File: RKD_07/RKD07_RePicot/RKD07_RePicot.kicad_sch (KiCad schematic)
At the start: 13 parts, among them J1 Conn_01x06, J2 Conn_01x24, J3 Qwiic_RA, J4 Conn_01x06, J5 Conn_01x02_Socket, J6 Conn_01x06, J8 Conn_01x06, SW41 SW_Push, U1 Pico

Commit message: modify
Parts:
- added J7: Conn_01x02_Socket, Connector_PinHeader_2.54mm:PinHeader_1x02_P2.54mm_Horizontal, symbol Connector_Generic:Conn_01x02
- J5: footprint Connector_PinHeader_2.54mm:PinHeader_1x02_P2.54mm_Vertical -> Connector_PinHeader_2.54mm:PinHeader_1x02_P2.54mm_Horizontal
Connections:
- net GP04: now also J7.1 (Pin_1)
- net GP07: now also J7.2 (Pin_2)
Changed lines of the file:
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@@
+		)
+	)
+	(global_label "GP04"
+		(shape input)
+		(at 298.45 120.65 180)
+		(fields_autoplaced yes)
+		(effects
+			(font
+				(size 1.27 1.27)
+			)
+			(justify right)
+		)
+		(property "Intersheetrefs" "${INTERSHEET_REFS}"
+			(at 290.5058 120.65 0)
+			(effects
+				(font
+					(size 1.27 1.27)
+				)
+				(justify right)
+				(hide yes)
+			)
 		)
 	)
@@
 				)
 				(justify left)
+				(hide yes)
+			)
+		)
+	)
+	(global_label "GP07"
+		(shape input)
+		(at 298.45 123.19 180)
+		(fields_autoplaced yes)
+		(effects
+			(font
+				(size 1.27 1.27)
+			)
+			(justify right)
+		)
+		(property "Intersheetrefs" "${INTERSHEET_REFS}"
+			(at 290.5058 123.19 0)
+			(effects
+				(font
+					(size 1.27 1.27)
+				)
+				(justify right)
 				(hide yes)
 			)
@@
 	)
 	(symbol
+		(lib_id "Connector_Generic:Conn_01x02")
+		(at 303.53 120.65 0)
+		(unit 1)
+		(exclude_from_sim no)
+		(in_bom yes)
+		(on_board yes)
+		(dnp no)
+		(fields_autoplaced yes)
+		(property "Reference" "J7"
+			(at 306.07 120.6499 0)
+			(effects
+				(font
+					(size 1.27 1.27)
+				)
+				(justify left)
+			)
+		)
+		(property "Value" "Conn_01x02_Socket"
+			(at 306.07 123.1899 0)
+			(effects
+				(font
+					(size 1.27 1.27)
+				)
+				(justify left)
+			)
+		)
+		(property "Footprint" "Connector_PinHeader_2.54mm:PinHeader_1x02_P2.54mm_Horizontal"
+			(at 303.53 120.65 0)
+			(effects
+				(font
+					(size 1.27 1.27)
+				)
+				(hide yes)
+			)
+		)
+		(property "Datasheet" "~"
+			(at 303.53 120.65 0)
+			(effects
+				(font
+					(size 1.27 1.27)
+				)
+				(hide yes)
+			)
+		)
+		(property "Description" "Generic connector, single row, 01x02, script generated (kicad-library-utils/schlib/autogen/connector/)"
+			(at 303.53 120.65 0)
+			(effects
+				(font
+					(size 1.27 1.27)
+				)
+				(hide yes)
+			)
+		)
+		(pin "1"
+		)
+		(pin "2"
+		)
+		(instances
+			(project "RKD07_RePicot"
+				(path "/237aa5e6-259c-459d-b408-55413a51412a"
+					(reference "J7")
+					(unit 1)
+				)
+			)
+		)
+	)
+	(symbol
 		(lib_id "SparkFun-Connector:Qwiic_Right_Angle")
 		(at 224.79 62.23 0)
@@
 			)
 		)
-		(property "Footprint" "Connector_PinHeader_2.54mm:PinHeader_1x02_P2.54mm_Vertical"
+		(property "Footprint" "Connector_PinHeader_2.54mm:PinHeader_1x02_P2.54mm_Horizontal"
 			(at 304.8 109.22 0)
 			(effects

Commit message: RePicot修正
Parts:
- added C1, C4: 0.1uF, Capacitor_SMD:C_0805_2012Metric_Pad1.18x1.45mm_HandSolder, symbol Device:C_Small
- added C2: 1uF, Capacitor_SMD:C_0805_2012Metric_Pad1.18x1.45mm_HandSolder, symbol Device:C_Small
- added C3: 4.7uF/10V, Capacitor_SMD:C_0805_2012Metric_Pad1.18x1.45mm_HandSolder, symbol Device:C_Small
- added J10, J11: Conn_01x02_Socket, Connector_PinHeader_2.54mm:PinHeader_1x02_P2.54mm_Horizontal, symbol Connector_Generic:Conn_01x02
- added J12: Conn_01x06, Connector_PinHeader_2.54mm:PinHeader_1x06_P2.54mm_Horizontal, symbol Connector_Generic:Conn_01x06
- added J9: Conn_01x06, Connector_FFC-FPC:Hirose_FH12-6S-0.5SH_1x06-1MP_P0.50mm_Horizontal, symbol Connector_Generic:Conn_01x06
- added R3, R5: 10k, Resistor_SMD:R_0805_2012Metric_Pad1.20x1.40mm_HandSolder, symbol Device:R
- added R4: 39R, Resistor_SMD:R_0805_2012Metric_Pad1.20x1.40mm_HandSolder, symbol Device:R
- added U2: TLV70019DDCR, Package_TO_SOT_SMD:SOT-23-5_HandSoldering, symbol Regulator_Linear:TLV70019_SOT23-5
- added U3: PMW3360DM-T2QU, Rikkodo_FootPrint:PMW3360DM-T2QU, symbol sumi-symbols:PMW3360DM-T2QU
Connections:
- net 3V3: now also C1.1, J12.6 (Pin_6), J9.1 (Pin_1), R3.2, R5.1, U2.1 (IN), U2.3 (EN), U3.5 (VDDIO)
- net GND: now also C1.2, C2.2, C3.2, C4.2, J12.1 (Pin_1), J12.2 (Pin_2), J9.6 (Pin_6), U2.2 (GND), U3.13 (NCS), U3.8 (GND)
- net GP00_MISO: now also J12.3 (Pin_3), J9.2 (Pin_2), R5.2, U3.12 (MISO)
- net GP02_SCLK: now also J12.4 (Pin_4), J9.4 (Pin_4), U3.10 (SCLK)
- net GP03_MOSI: now also J12.5 (Pin_5), J9.5 (Pin_5), U3.11 (MOSI)
- new net: C3.1, C4.1, U3.3 (VDDPIX)
- new net: R3.1, U3.7 (NRESET)
- new net: R4.2, U3.15 (LED_P)
- new net +1V9: C2.1, R4.1, U2.5 (OUT), U3.4 (VDD)
- new net GP04_F: J10.1 (Pin_1), J11.2 (Pin_2)
- new net GP07_F: J10.2 (Pin_2), J11.1 (Pin_1)
- no-connect marks 14 -> 16
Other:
- note added: "Nogikesuya_TrackBall"
- moved on the sheet: D41, J1, J2, J3, J4, J6, J8, OL1, R1, R2, SW41

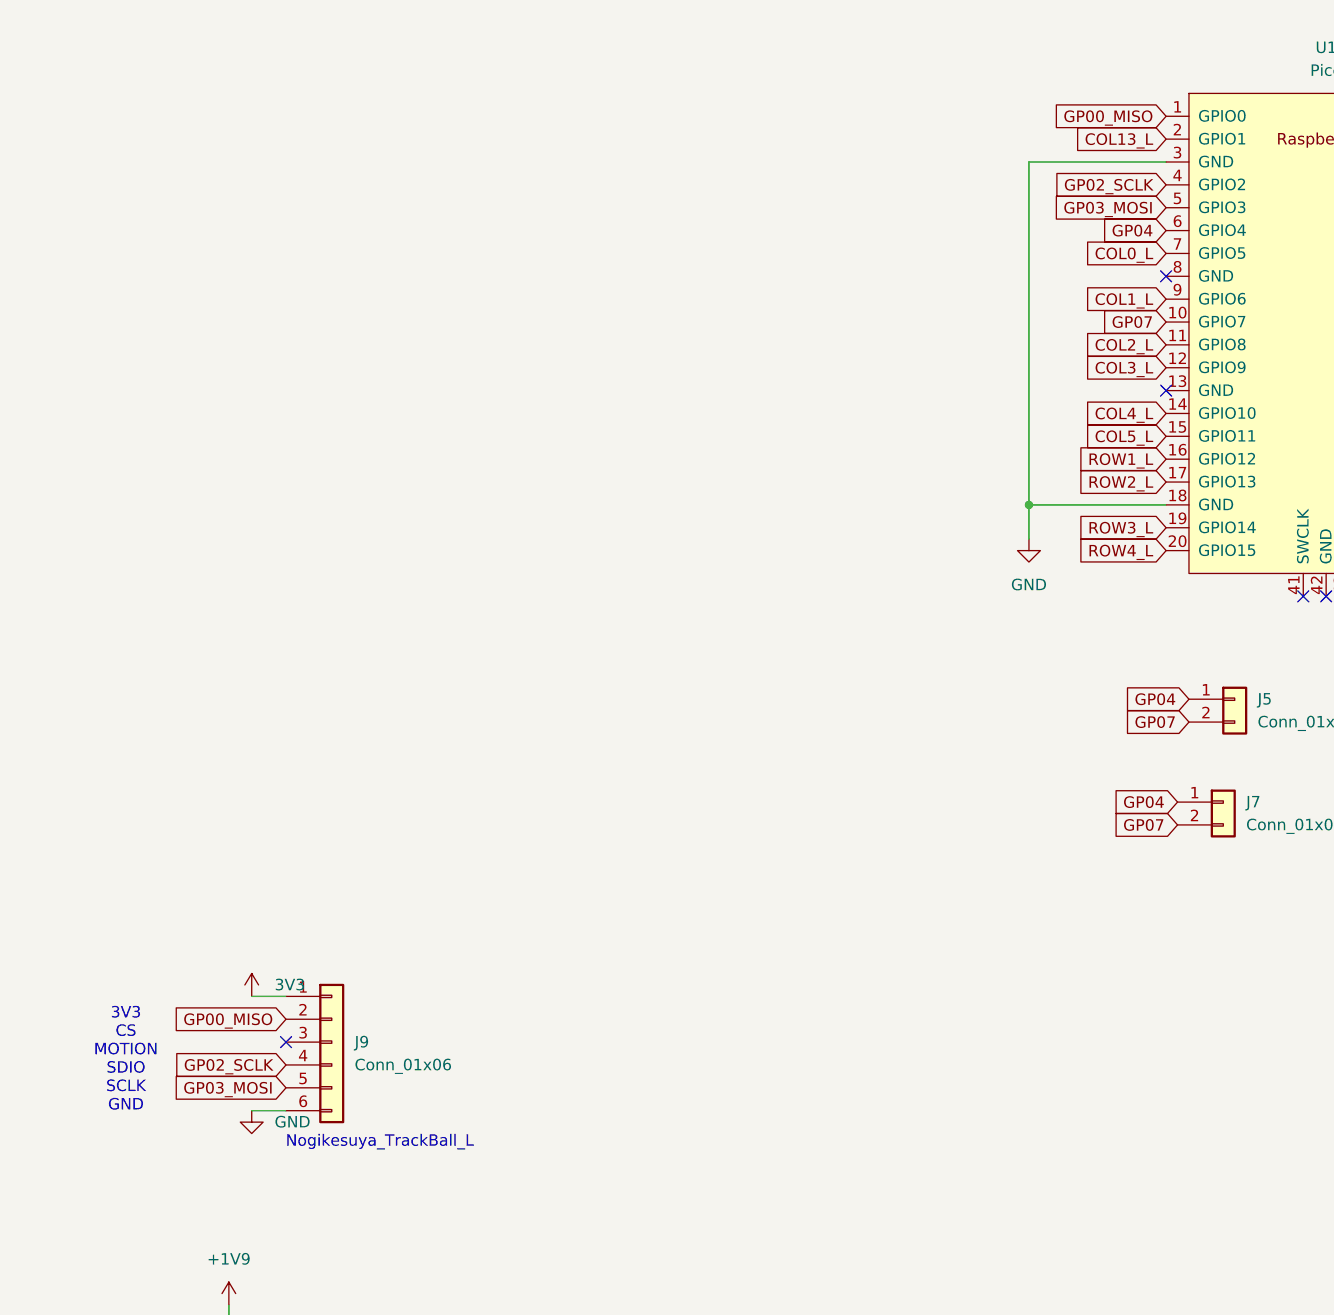
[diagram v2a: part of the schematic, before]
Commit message: Add NogikesuTrackpad
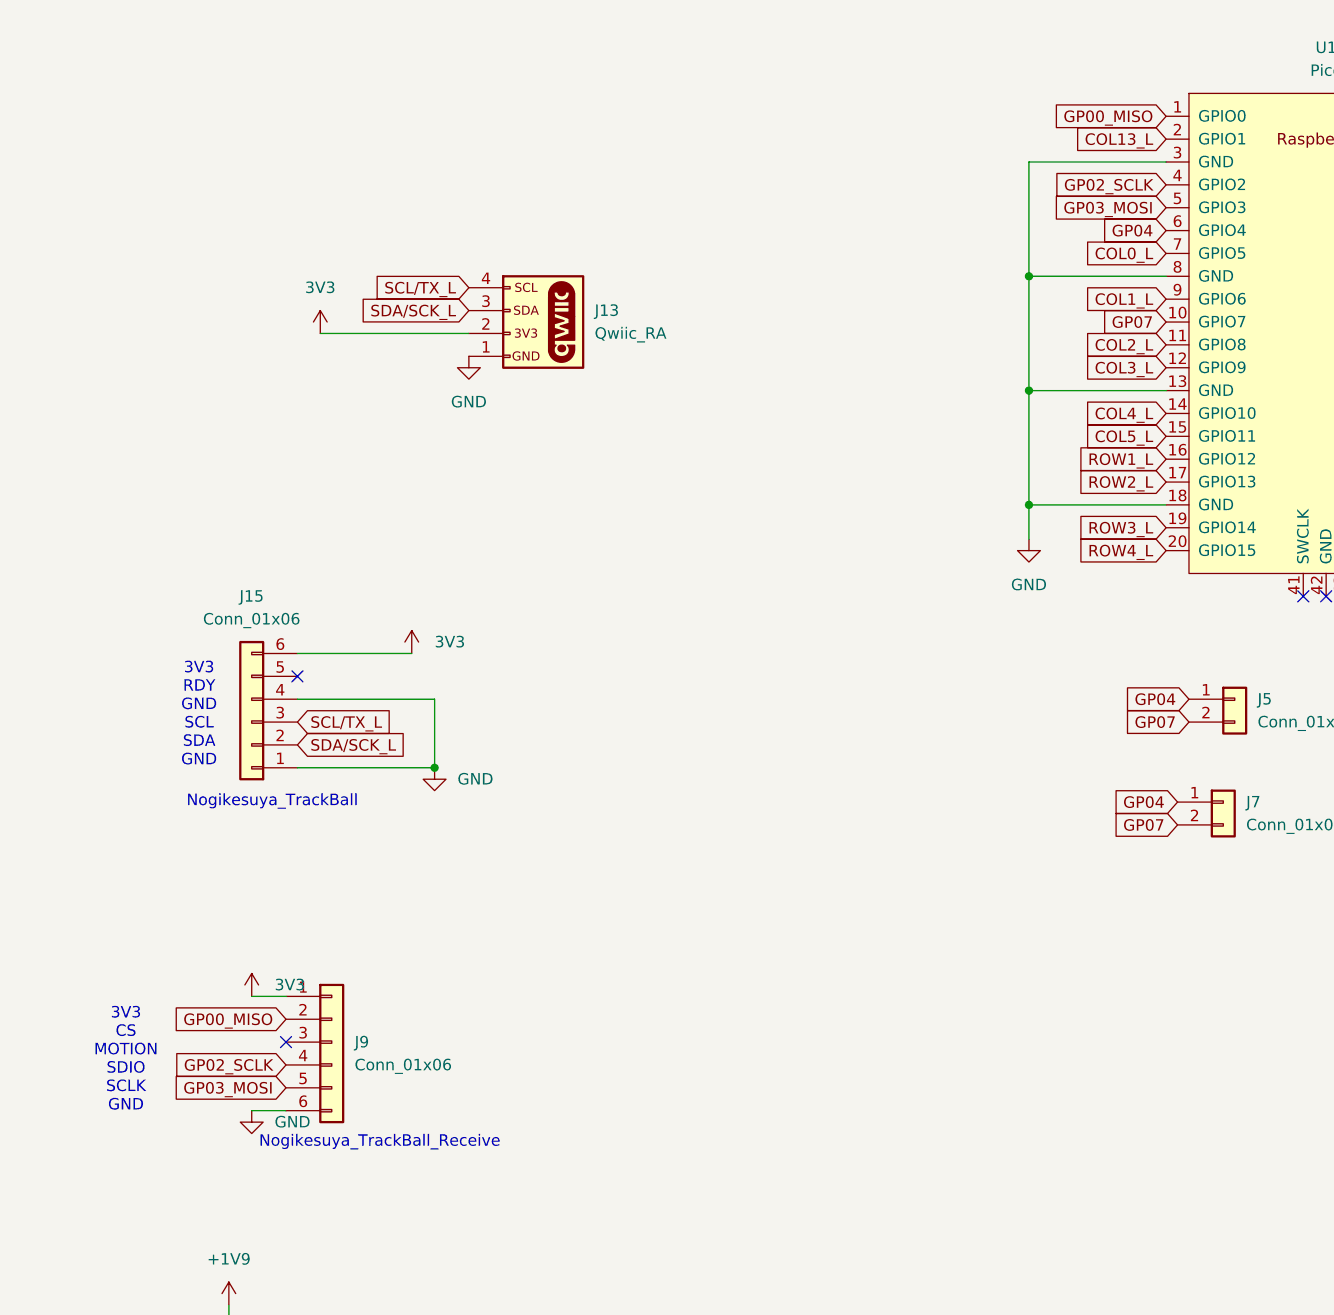
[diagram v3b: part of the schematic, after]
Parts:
- added J13: Qwiic_RA, SparkFun-Connector:JST_SMD_1.0mm-4_Black, symbol SparkFun-Connector:Qwiic_Right_Angle
- added J15: Conn_01x06, Connector_FFC-FPC:Hirose_FH12-6S-0.5SH_1x06-1MP_P0.50mm_Horizontal, symbol Connector_Generic:Conn_01x06
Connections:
- net 3V3: now also J13.2 (Pin_2), J15.6 (Pin_6)
- net GND: now also U1.13 (GND), U1.8 (GND), J13.1 (Pin_1), J15.1 (Pin_1), J15.4 (Pin_4)
- net SCL/TX_L: now also J13.4 (Pin_4), J15.3 (Pin_3)
- net SDA/SCK_L: now also J13.3 (Pin_3), J15.2 (Pin_2)
- no-connect marks 16 -> 15
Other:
- note added: "3V3 RDY GND SCL SDA GND"
- note added: "Nogikesuya_TrackBall_Receive"
- note removed: "Nogikesuya_TrackBall_L"
